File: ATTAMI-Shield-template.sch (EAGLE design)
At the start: 3 parts, among them J1 CON_HEADER_1X02-PTH, J3 CON_HEADER_1X02-PTH, J4 CON_HEADER_1X06-PTH

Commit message: template for v17
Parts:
- removed J4: CON_HEADER_1X06-PTH, dp_devices:CON_HEADER_1X06-PTH
- added J2: (no value), microbuilder:HEADER-1X2ROUND
- J1: value CON_HEADER_1X02-PTH -> (none); device dp_devices:CON_HEADER_1X02-PTH -> microbuilder:HEADER-1X2ROUND
- J3: value CON_HEADER_1X02-PTH -> (none); device dp_devices:CON_HEADER_1X02-PTH -> microbuilder:HEADER-1X7ROUND
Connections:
- new net GND: J1.2, J2.2, J3.1
- new net PB0: J3.2
- new net PB1: J3.3
- new net PB2: J3.4
- new net PB3: J3.5
- new net PB4: J3.6
- new net PB5: J3.7
- new net VBAT: J1.1
- new net VCC: J2.1
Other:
- note added: "T.A.M.I hackerspace crew Shield proto LICENSE: CERN OHL 1.7"
- note removed: "AT TAMI Ver. 15b03"
- note removed: "ATtami ver1 Shield Base"
- note removed: "T.A.M.I hackerspace crew LICENSE: CERN OHL 1.7"
- note removed: "refer to V15b06"
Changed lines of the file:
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@@
 <setting verticaltext="up"/>
 </settings>
-<grid distance="0.1" unitdist="inch" unit="inch" style="lines" multiple="1" display="no" altdistance="0.01" altunitdist="inch" altunit="inch"/>
+<grid distance="0.05" unitdist="inch" unit="inch" style="lines" multiple="1" display="no" altdistance="0.01" altunitdist="inch" altunit="inch"/>
 <layers>
 <layer number="1" name="Top" color="4" fill="1" visible="no" active="no"/>
@@
 </classes>
 <parts>
-<part name="J1" library="dp_devices" deviceset="CON_HEADER_1X02" device="-PTH"/>
-<part name="J3" library="dp_devices" deviceset="CON_HEADER_1X02" device="-PTH"/>
-<part name="J4" library="dp_devices" deviceset="CON_HEADER_1X06" device="-PTH"/>
+<part name="GND16" library="SparkFun" deviceset="GND" device=""/>
+<part name="GND1" library="SparkFun" deviceset="GND" device=""/>
+<part name="J1" library="microbuilder" deviceset="HEADER-1X2" device="ROUND"/>
+<part name="J2" library="microbuilder" deviceset="HEADER-1X2" device="ROUND"/>
+<part name="FRAME1" library="frames" deviceset="A4L-LOC" device=""/>
+<part name="J3" library="microbuilder" deviceset="HEADER-1X7" device="ROUND"/>
+<part name="GND5" library="SparkFun" deviceset="GND" device=""/>
 </parts>
 <sheets>
@@
 <vertex x="0.3796875" y="-0.91665"/>
 </polygon>
-<frame x1="-2.54" y1="-25.4" x2="266.7" y2="185.42" columns="8" rows="5" layer="100"/>
-<text x="205.74" y="0" size="2.54" layer="100" font="vector">T.A.M.I hackerspace crew
-LICENSE: CERN OHL 1.7</text>
-<text x="205.74" y="-7.62" size="2.54" layer="100" font="vector">AT TAMI Ver. 15b03</text>
-<text x="205.74" y="-15.24" size="2.54" layer="100" font="vector">&gt;LAST_DATE_TIME</text>
-<wire x1="198.12" y1="-20.32" x2="198.12" y2="17.78" width="0.254" layer="100"/>
-<wire x1="198.12" y1="17.78" x2="261.62" y2="17.78" width="0.254" layer="100"/>
-<text x="66.04" y="27.94" size="6.4516" layer="100" rot="R180">ATtami ver1
-Shield Base</text>
-<text x="20.32" y="-5.08" size="6.4516" layer="100">refer to V15b06</text>
+<text x="162.56" y="6.35" size="2.54" layer="100" font="vector">T.A.M.I hackerspace crew
+Shield proto
+LICENSE: CERN OHL 1.7
+</text>
 </plain>
 <instances>
-<instance part="J1" gate="J" x="83.82" y="147.32" rot="MR0"/>
-<instance part="J3" gate="J" x="83.82" y="162.56" rot="MR0"/>
-<instance part="J4" gate="G$1" x="172.72" y="154.94"/>
+<instance part="GND16" gate="1" x="43.18" y="119.38"/>
+<instance part="GND1" gate="1" x="166.37" y="116.84"/>
+<instance part="J1" gate="G$1" x="156.21" y="121.92" rot="MR0"/>
+<instance part="J2" gate="G$1" x="33.02" y="124.46" rot="MR0"/>
+<instance part="FRAME1" gate="G$1" x="0" y="0"/>
+<instance part="J3" gate="A" x="165.1" y="85.09"/>
+<instance part="GND5" gate="1" x="154.94" y="100.33" rot="R180"/>
 </instances>
 <busses>
 </busses>
 <nets>
+<net name="GND" class="0">
+<segment>
+<pinref part="GND16" gate="1" pin="GND"/>
+<wire x1="43.18" y1="124.46" x2="43.18" y2="121.92" width="0.1524" layer="91"/>
+<pinref part="J2" gate="G$1" pin="2"/>
+<wire x1="43.18" y1="124.46" x2="35.56" y2="124.46" width="0.1524" layer="91"/>
+</segment>
+<segment>
+<wire x1="158.75" y1="121.92" x2="166.37" y2="121.92" width="0.1524" layer="91"/>
+<wire x1="166.37" y1="121.92" x2="166.37" y2="119.38" width="0.1524" layer="91"/>
+<pinref part="GND1" gate="1" pin="GND"/>
+<pinref part="J1" gate="G$1" pin="2"/>
+</segment>
+<segment>
+<pinref part="J3" gate="A" pin="1"/>
+<wire x1="162.56" y1="92.71" x2="154.94" y2="92.71" width="0.1524" layer="91"/>
+<wire x1="154.94" y1="92.71" x2="154.94" y2="97.79" width="0.1524" layer="91"/>
+<pinref part="GND5" gate="1" pin="GND"/>
+</segment>
+</net>
+<net name="VCC" class="0">
+<segment>
+<pinref part="J2" gate="G$1" pin="1"/>
+<wire x1="35.56" y1="127" x2="43.18" y2="127" width="0.1524" layer="91"/>
+<label x="43.18" y="127" size="1.778" layer="95"/>
+</segment>
+</net>
+<net name="VBAT" class="0">
+<segment>
+<pinref part="J1" gate="G$1" pin="1"/>
+<wire x1="165.1" y1="124.46" x2="158.75" y2="124.46" width="0.1524" layer="91"/>
+<label x="163.83" y="125.73" size="1.778" layer="95"/>
+</segment>
+</net>
+<net name="PB3" class="0">
+<segment>
+<pinref part="J3" gate="A" pin="5"/>
+<wire x1="162.56" y1="82.55" x2="156.21" y2="82.55" width="0.1524" layer="91"/>
+<label x="153.67" y="82.55" size="1.778" layer="95"/>
+</segment>
+</net>
+<net name="PB4" class="0">
+<segment>
+<pinref part="J3" gate="A" pin="6"/>
+<wire x1="162.56" y1="80.01" x2="156.21" y2="80.01" width="0.1524" layer="91"/>
+<label x="153.67" y="80.01" size="1.778" layer="95"/>
+</segment>
+</net>
+<net name="PB5" class="0">
+<segment>
+<pinref part="J3" gate="A" pin="7"/>
+<wire x1="162.56" y1="77.47" x2="156.21" y2="77.47" width="0.1524" layer="91"/>
+<label x="153.67" y="77.47" size="1.778" layer="95"/>
+</segment>
+</net>
+<net name="PB1" class="0">
+<segment>
+<pinref part="J3" gate="A" pin="3"/>
+<wire x1="162.56" y1="87.63" x2="153.67" y2="87.63" width="0.1524" layer="91"/>
+<label x="153.67" y="87.63" size="1.778" layer="95"/>
+</segment>
+</net>
+<net name="PB2" class="0">
+<segment>
+<pinref part="J3" gate="A" pin="4"/>
+<wire x1="162.56" y1="85.09" x2="153.67" y2="85.09" width="0.1524" layer="91"/>
+<label x="153.67" y="85.09" size="1.778" layer="95"/>
+</segment>
+</net>
+<net name="PB0" class="0">
+<segment>
+<pinref part="J3" gate="A" pin="2"/>
+<wire x1="162.56" y1="90.17" x2="153.67" y2="90.17" width="0.1524" layer="91"/>
+</segment>
+</net>
 </nets>
 </sheet>

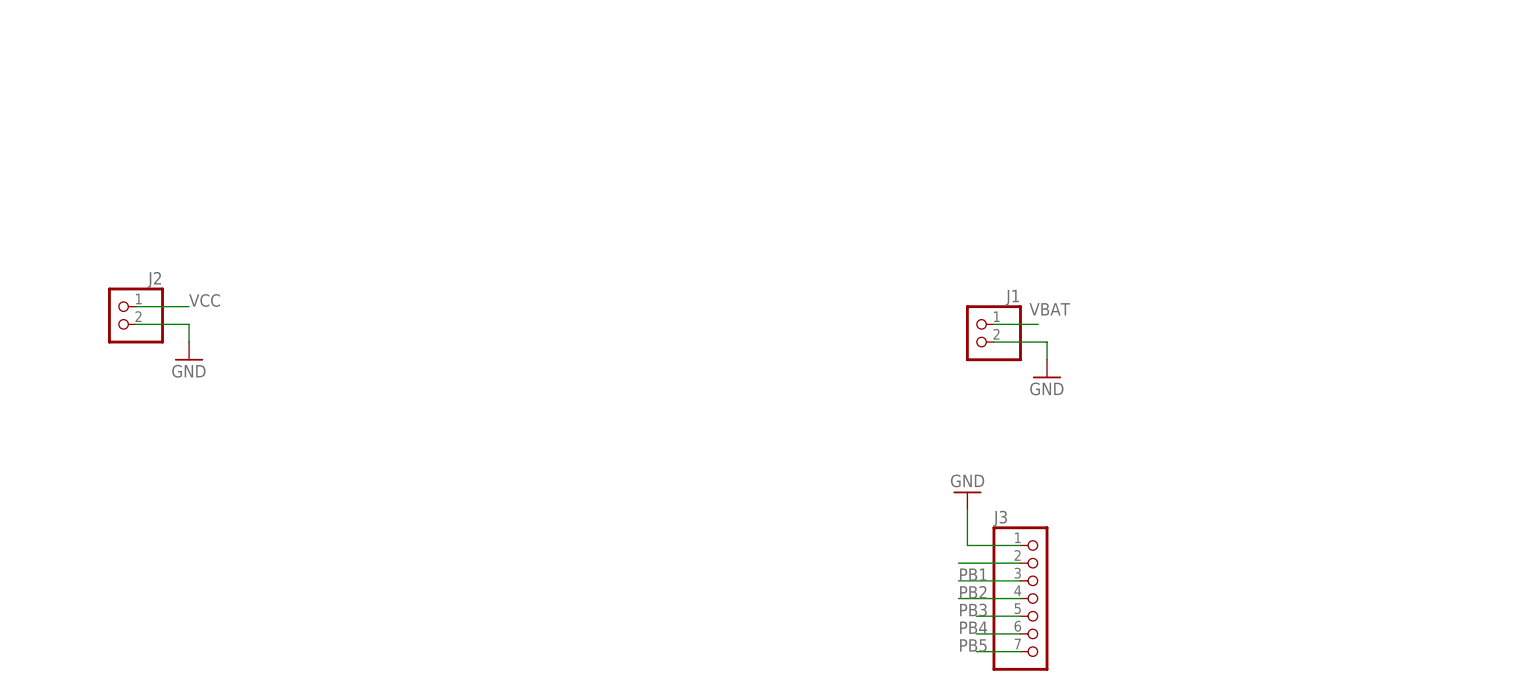
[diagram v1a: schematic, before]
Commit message: same shield, with added mounting holes and better naming based on ver 0.00
based on attami ver 0.00

https://github.com/telavivmakers/at-tami/commit/00271a633f93de088d04ac549667f0e04d0c47cf#diff-2c24cc5344d8d061ae0f0b1c47d7ba8a
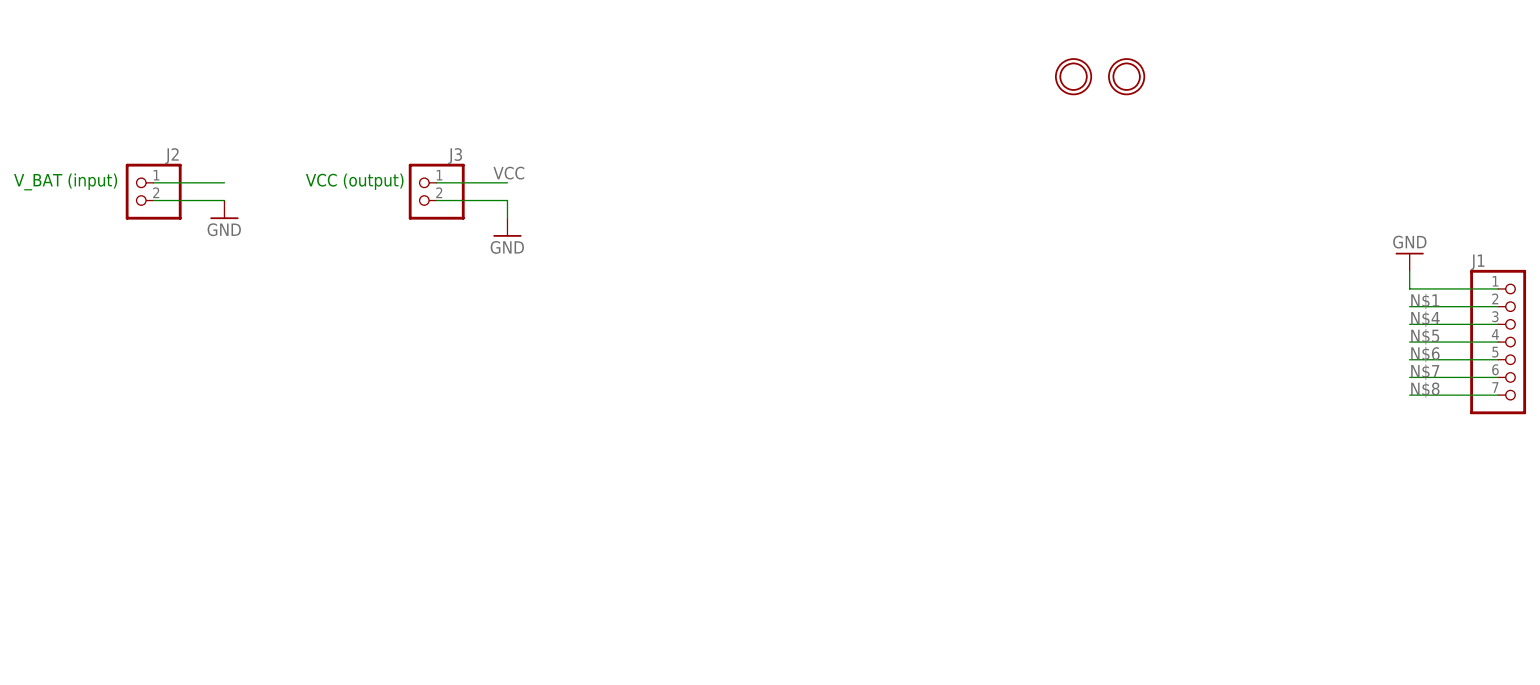
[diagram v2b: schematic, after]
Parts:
- added U$1, U$2: MOUNTINGHOLE2.0, microbuilder:MOUNTINGHOLE2.0
- J1: device microbuilder:HEADER-1X2ROUND -> microbuilder:HEADER-1X7ROUND
- J3: device microbuilder:HEADER-1X7ROUND -> microbuilder:HEADER-1X2ROUND
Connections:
- removed net PB0: J3.2
- removed net PB1: J3.3
- removed net PB2: J3.4
- removed net PB3: J3.5
- removed net PB4: J3.6
- removed net PB5: J3.7
- removed net VBAT: J1.1
- new net N$1: J1.2
- new net N$3: J2.1
- new net N$4: J1.3
- new net N$5: J1.4
- new net N$6: J1.5
- new net N$7: J1.6
- new net N$8: J1.7
- net GND: now also J1.1, J3.2; no longer J1.2, J3.1
- net VCC: now also J3.1; no longer J2.1
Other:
- note added: "T.A.M.I hackerspace crew LICENSE: CERN OHL 1.7"
- note added: "VCC (output)"
- note added: "V_BAT (input)"
- note added: "more at github.com/telavivmakers/at-tami Notes: 1. D1 and D2 are Blue LEDs they might not light when using Vi_BAT <4V~ 2. When VCC is less than 5V change the system clock of the ATTINY85 to 8MHz or less - refer to the datasheet P163 Section 21-3 Speed"
- note removed: "T.A.M.I hackerspace crew Shield proto LICENSE: CERN OHL 1.7"
- moved on the sheet: J2
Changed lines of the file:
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@@
 <?xml version="1.0" encoding="utf-8"?>
 <!DOCTYPE eagle SYSTEM "eagle.dtd">
-<eagle version="6.5.0">
+<eagle version="7.1.0">
 <drawing>
 <settings>
@@
 <setting verticaltext="up"/>
 </settings>
-<grid distance="0.05" unitdist="inch" unit="inch" style="lines" multiple="1" display="no" altdistance="0.01" altunitdist="inch" altunit="inch"/>
+<grid distance="0.1" unitdist="inch" unit="inch" style="lines" multiple="1" display="no" altdistance="0.01" altunitdist="inch" altunit="inch"/>
 <layers>
 <layer number="1" name="Top" color="4" fill="1" visible="no" active="no"/>
@@
 <part name="GND16" library="SparkFun" deviceset="GND" device=""/>
 <part name="GND1" library="SparkFun" deviceset="GND" device=""/>
-<part name="J1" library="microbuilder" deviceset="HEADER-1X2" device="ROUND"/>
+<part name="U$1" library="microbuilder" deviceset="MOUNTINGHOLE" device="2.0" value="MOUNTINGHOLE2.0"/>
+<part name="U$2" library="microbuilder" deviceset="MOUNTINGHOLE" device="2.0" value="MOUNTINGHOLE2.0"/>
 <part name="J2" library="microbuilder" deviceset="HEADER-1X2" device="ROUND"/>
+<part name="J3" library="microbuilder" deviceset="HEADER-1X2" device="ROUND"/>
 <part name="FRAME1" library="frames" deviceset="A4L-LOC" device=""/>
-<part name="J3" library="microbuilder" deviceset="HEADER-1X7" device="ROUND"/>
+<part name="J1" library="microbuilder" deviceset="HEADER-1X7" device="ROUND"/>
 <part name="GND5" library="SparkFun" deviceset="GND" device=""/>
 </parts>
@@
 <sheet>
 <plain>
+<text x="33.02" y="33.02" size="1.778" layer="100">more at  github.com/telavivmakers/at-tami
+Notes:
+1. D1 and D2 are Blue LEDs they might  not light when using  Vi_BAT &lt;4V~
+2. When VCC is less than 5V change the system clock of the ATTINY85 to 8MHz or less -
+refer to the datasheet  P163 Section  21-3 Speed</text>
 <polygon width="0.254" layer="21">
 <vertex x="0.83533125" y="-2.01666875" curve="9.500029"/>
@@
 <vertex x="0.3796875" y="-0.91665"/>
 </polygon>
-<text x="162.56" y="6.35" size="2.54" layer="100" font="vector">T.A.M.I hackerspace crew
-Shield proto
-LICENSE: CERN OHL 1.7
-</text>
+<text x="165.1" y="12.7" size="2.54" layer="100" font="vector">T.A.M.I hackerspace crew
+LICENSE: CERN OHL 1.7</text>
+<text x="59.944" y="144.272" size="1.778" layer="91">VCC (output)</text>
+<text x="18.034" y="144.272" size="1.778" layer="91">V_BAT (input)</text>
 </plain>
 <instances>
-<instance part="GND16" gate="1" x="43.18" y="119.38"/>
-<instance part="GND1" gate="1" x="166.37" y="116.84"/>
-<instance part="J1" gate="G$1" x="156.21" y="121.92" rot="MR0"/>
-<instance part="J2" gate="G$1" x="33.02" y="124.46" rot="MR0"/>
+<instance part="GND16" gate="1" x="88.9" y="137.16"/>
+<instance part="GND1" gate="1" x="48.26" y="139.7"/>
+<instance part="U$1" gate="G$1" x="177.8" y="160.02"/>
+<instance part="U$2" gate="G$1" x="170.18" y="160.02"/>
+<instance part="J2" gate="G$1" x="35.56" y="142.24" rot="MR0"/>
+<instance part="J3" gate="G$1" x="76.2" y="142.24" rot="MR0"/>
 <instance part="FRAME1" gate="G$1" x="0" y="0"/>
-<instance part="J3" gate="A" x="165.1" y="85.09"/>
-<instance part="GND5" gate="1" x="154.94" y="100.33" rot="R180"/>
+<instance part="J1" gate="A" x="233.68" y="121.92"/>
+<instance part="GND5" gate="1" x="218.44" y="134.62" rot="R180"/>
 </instances>
 <busses>
@@
 <segment>
 <pinref part="GND16" gate="1" pin="GND"/>
-<wire x1="43.18" y1="124.46" x2="43.18" y2="121.92" width="0.1524" layer="91"/>
+<wire x1="88.9" y1="142.24" x2="88.9" y2="139.7" width="0.1524" layer="91"/>
+<pinref part="J3" gate="G$1" pin="2"/>
+<wire x1="88.9" y1="142.24" x2="78.74" y2="142.24" width="0.1524" layer="91"/>
+</segment>
+<segment>
+<wire x1="38.1" y1="142.24" x2="48.26" y2="142.24" width="0.1524" layer="91"/>
+<pinref part="GND1" gate="1" pin="GND"/>
 <pinref part="J2" gate="G$1" pin="2"/>
-<wire x1="43.18" y1="124.46" x2="35.56" y2="124.46" width="0.1524" layer="91"/>
-</segment>
-<segment>
-<wire x1="158.75" y1="121.92" x2="166.37" y2="121.92" width="0.1524" layer="91"/>
-<wire x1="166.37" y1="121.92" x2="166.37" y2="119.38" width="0.1524" layer="91"/>
-<pinref part="GND1" gate="1" pin="GND"/>
-<pinref part="J1" gate="G$1" pin="2"/>
-</segment>
-<segment>
-<pinref part="J3" gate="A" pin="1"/>
-<wire x1="162.56" y1="92.71" x2="154.94" y2="92.71" width="0.1524" layer="91"/>
-<wire x1="154.94" y1="92.71" x2="154.94" y2="97.79" width="0.1524" layer="91"/>
+</segment>
+<segment>
+<pinref part="J1" gate="A" pin="1"/>
+<wire x1="231.14" y1="129.54" x2="218.44" y2="129.54" width="0.1524" layer="91"/>
+<wire x1="218.44" y1="129.54" x2="218.44" y2="132.08" width="0.1524" layer="91"/>
 <pinref part="GND5" gate="1" pin="GND"/>
 </segment>
@@
 <net name="VCC" class="0">
 <segment>
+<pinref part="J3" gate="G$1" pin="1"/>
+<wire x1="88.9" y1="144.78" x2="78.74" y2="144.78" width="0.1524" layer="91"/>
+<label x="86.868" y="145.288" size="1.778" layer="95"/>
+</segment>
+</net>
+<net name="N$3" class="0">
+<segment>
 <pinref part="J2" gate="G$1" pin="1"/>
-<wire x1="35.56" y1="127" x2="43.18" y2="127" width="0.1524" layer="91"/>
-<label x="43.18" y="127" size="1.778" layer="95"/>
-</segment>
-</net>
-<net name="VBAT" class="0">
-<segment>
-<pinref part="J1" gate="G$1" pin="1"/>
-<wire x1="165.1" y1="124.46" x2="158.75" y2="124.46" width="0.1524" layer="91"/>
-<label x="163.83" y="125.73" size="1.778" layer="95"/>
-</segment>
-</net>
-<net name="PB3" class="0">
-<segment>
-<pinref part="J3" gate="A" pin="5"/>
-<wire x1="162.56" y1="82.55" x2="156.21" y2="82.55" width="0.1524" layer="91"/>
-<label x="153.67" y="82.55" size="1.778" layer="95"/>
-</segment>
-</net>
-<net name="PB4" class="0">
-<segment>
-<pinref part="J3" gate="A" pin="6"/>
-<wire x1="162.56" y1="80.01" x2="156.21" y2="80.01" width="0.1524" layer="91"/>
-<label x="153.67" y="80.01" size="1.778" layer="95"/>
-</segment>
-</net>
-<net name="PB5" class="0">
-<segment>
-<pinref part="J3" gate="A" pin="7"/>
-<wire x1="162.56" y1="77.47" x2="156.21" y2="77.47" width="0.1524" layer="91"/>
-<label x="153.67" y="77.47" size="1.778" layer="95"/>
-</segment>
-</net>
-<net name="PB1" class="0">
-<segment>
-<pinref part="J3" gate="A" pin="3"/>
-<wire x1="162.56" y1="87.63" x2="153.67" y2="87.63" width="0.1524" layer="91"/>
-<label x="153.67" y="87.63" size="1.778" layer="95"/>
-</segment>
-</net>
-<net name="PB2" class="0">
-<segment>
-<pinref part="J3" gate="A" pin="4"/>
-<wire x1="162.56" y1="85.09" x2="153.67" y2="85.09" width="0.1524" layer="91"/>
-<label x="153.67" y="85.09" size="1.778" layer="95"/>
-</segment>
-</net>
-<net name="PB0" class="0">
-<segment>
-<pinref part="J3" gate="A" pin="2"/>
-<wire x1="162.56" y1="90.17" x2="153.67" y2="90.17" width="0.1524" layer="91"/>
+<wire x1="38.1" y1="144.78" x2="48.26" y2="144.78" width="0.1524" layer="91"/>
+</segment>
+</net>
+<net name="N$1" class="0">
+<segment>
+<pinref part="J1" gate="A" pin="2"/>
+<wire x1="231.14" y1="127" x2="218.44" y2="127" width="0.1524" layer="91"/>
+<label x="218.44" y="127" size="1.778" layer="95"/>
+</segment>
+</net>
+<net name="N$4" class="0">
+<segment>
+<pinref part="J1" gate="A" pin="3"/>
+<wire x1="231.14" y1="124.46" x2="218.44" y2="124.46" width="0.1524" layer="91"/>
+<label x="218.44" y="124.46" size="1.778" layer="95"/>
+</segment>
+</net>
+<net name="N$5" class="0">
+<segment>
+<pinref part="J1" gate="A" pin="4"/>
+<wire x1="231.14" y1="121.92" x2="218.44" y2="121.92" width="0.1524" layer="91"/>
+<label x="218.44" y="121.92" size="1.778" layer="95"/>
+</segment>
+</net>
+<net name="N$6" class="0">
+<segment>
+<pinref part="J1" gate="A" pin="5"/>
+<wire x1="218.44" y1="119.38" x2="231.14" y2="119.38" width="0.1524" layer="91"/>
+<label x="218.44" y="119.38" size="1.778" layer="95"/>
+</segment>
+</net>
+<net name="N$7" class="0">
+<segment>
+<pinref part="J1" gate="A" pin="6"/>
+<wire x1="218.44" y1="116.84" x2="231.14" y2="116.84" width="0.1524" layer="91"/>
+<label x="218.44" y="116.84" size="1.778" layer="95"/>
+</segment>
+</net>
+<net name="N$8" class="0">
+<segment>
+<pinref part="J1" gate="A" pin="7"/>
+<wire x1="218.44" y1="114.3" x2="231.14" y2="114.3" width="0.1524" layer="91"/>
+<label x="218.44" y="114.3" size="1.778" layer="95"/>
 </segment>
 </net>
@@
 </sheet>
 </sheets>
-<errors>
-</errors>
 </schematic>
 </drawing>

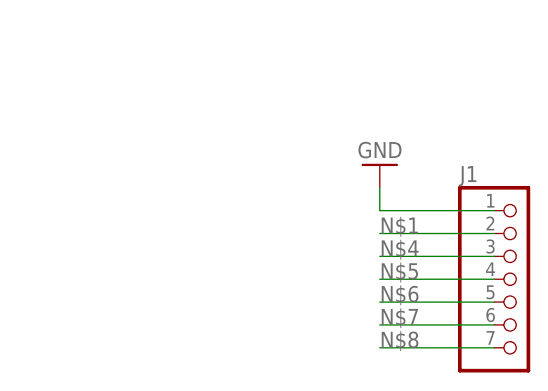
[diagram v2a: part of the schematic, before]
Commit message: servo shield - new
also added names and labels on wires
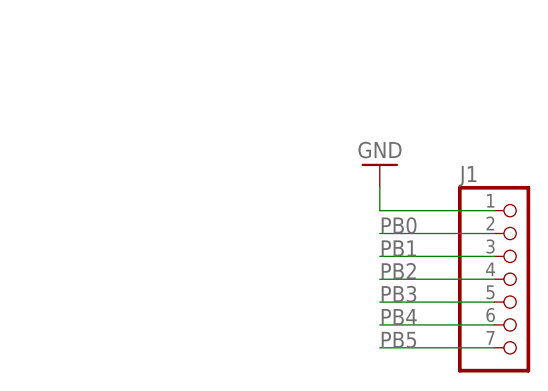
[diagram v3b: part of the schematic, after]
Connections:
- net N$1 renamed PB0
- net N$4 renamed PB1
- net N$5 renamed PB2
- net N$6 renamed PB3
- net N$7 renamed PB4
- net N$8 renamed PB5
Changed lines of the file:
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@@
 </segment>
 </net>
-<net name="N$1" class="0">
+<net name="PB0" class="0">
 <segment>
 <pinref part="J1" gate="A" pin="2"/>
@@
 </segment>
 </net>
-<net name="N$4" class="0">
+<net name="PB1" class="0">
 <segment>
 <pinref part="J1" gate="A" pin="3"/>
@@
 </segment>
 </net>
-<net name="N$5" class="0">
+<net name="PB2" class="0">
 <segment>
 <pinref part="J1" gate="A" pin="4"/>
@@
 </segment>
 </net>
-<net name="N$6" class="0">
+<net name="PB3" class="0">
 <segment>
 <pinref part="J1" gate="A" pin="5"/>
@@
 </segment>
 </net>
-<net name="N$7" class="0">
+<net name="PB4" class="0">
 <segment>
 <pinref part="J1" gate="A" pin="6"/>
@@
 </segment>
 </net>
-<net name="N$8" class="0">
+<net name="PB5" class="0">
 <segment>
 <pinref part="J1" gate="A" pin="7"/>
